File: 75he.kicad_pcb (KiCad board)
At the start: 2 copper layers, 325.3 x 138.7 mm, 395 parts, among them K1 DRV5055A3xDBZxQ1, K10 DRV5055A3xDBZxQ1, K11 DRV5055A3xDBZxQ1, K12 DRV5055A3xDBZxQ1, K13 DRV5055A3xDBZxQ1, K14 DRV5055A3xDBZxQ1, K15 DRV5055A3xDBZxQ1, K16 DRV5055A3xDBZxQ1, K17 DRV5055A3xDBZxQ1, K18 DRV5055A3xDBZxQ1, K19 DRV5055A3xDBZxQ1, K2 DRV5055A3xDBZxQ1, K20 DRV5055A3xDBZxQ1, K21 DRV5055A3xDBZxQ1, K22 DRV5055A3xDBZxQ1, K23 DRV5055A3xDBZxQ1, K24 DRV5055A3xDBZxQ1, K25 DRV5055A3xDBZxQ1, K26 DRV5055A3xDBZxQ1, K27 DRV5055A3xDBZxQ1, K28 DRV5055A3xDBZxQ1, K29 DRV5055A3xDBZxQ1, K3 DRV5055A3xDBZxQ1, K30 DRV5055A3xDBZxQ1, K31 DRV5055A3xDBZxQ1, K32 DRV5055A3xDBZxQ1, K33 DRV5055A3xDBZxQ1, K34 DRV5055A3xDBZxQ1, K35 DRV5055A3xDBZxQ1, K36 DRV5055A3xDBZxQ1, K37 DRV5055A3xDBZxQ1, K38 DRV5055A3xDBZxQ1, K39 DRV5055A3xDBZxQ1, K4 DRV5055A3xDBZxQ1, K40 DRV5055A3xDBZxQ1, K41 DRV5055A3xDBZxQ1, K42 DRV5055A3xDBZxQ1, K43 DRV5055A3xDBZxQ1, K44 DRV5055A3xDBZxQ1, K45 DRV5055A3xDBZxQ1, K46 DRV5055A3xDBZxQ1, K47 DRV5055A3xDBZxQ1, K48 DRV5055A3xDBZxQ1, K49 DRV5055A3xDBZxQ1, K5 DRV5055A3xDBZxQ1, K50 DRV5055A3xDBZxQ1, K51 DRV5055A3xDBZxQ1, K52 DRV5055A3xDBZxQ1, K53 DRV5055A3xDBZxQ1, K54 DRV5055A3xDBZxQ1, K55 DRV5055A3xDBZxQ1, K56 DRV5055A3xDBZxQ1, K57 DRV5055A3xDBZxQ1, K58 DRV5055A3xDBZxQ1, K59 DRV5055A3xDBZxQ1, K6 DRV5055A3xDBZxQ1, K60 DRV5055A3xDBZxQ1, K61 DRV5055A3xDBZxQ1, K62 DRV5055A3xDBZxQ1, K63 DRV5055A3xDBZxQ1, K64 DRV5055A3xDBZxQ1, K65 DRV5055A3xDBZxQ1, K66 DRV5055A3xDBZxQ1, K67 DRV5055A3xDBZxQ1, K68 DRV5055A3xDBZxQ1, K69 DRV5055A3xDBZxQ1, K7 DRV5055A3xDBZxQ1, K70 DRV5055A3xDBZxQ1, K71 DRV5055A3xDBZxQ1, K72 DRV5055A3xDBZxQ1, K73 DRV5055A3xDBZxQ1, K74 DRV5055A3xDBZxQ1, K75 DRV5055A3xDBZxQ1, K76 DRV5055A3xDBZxQ1, K77 DRV5055A3xDBZxQ1, K78 DRV5055A3xDBZxQ1, K79 DRV5055A3xDBZxQ1, K8 DRV5055A3xDBZxQ1, K80 DRV5055A3xDBZxQ1, K81 DRV5055A3xDBZxQ1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

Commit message: start usb
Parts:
- C172, SW_RST1: moved to B.Cu
- moved C172 115.0 mm to (147.6, 44.0)
- moved SW_RST1 86.5 mm to (147.6, 40.3), turned to -90 degrees
- moved C169 0.11 mm to (141.1, 41.4)
- moved C170 0.10 mm to (141.6, 39.9)
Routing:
- net /MCU/OSC_OUT: track 0.00 -> 6.83 mm
- net +3.3V: track 0.00 -> 5.15 mm
- net /MCU/OSC_IN: track 0.00 -> 4.32 mm
- net M6_OUT: track 216.6 -> 215.1 mm
- net M4_OUT: track 184.6 -> 185.8 mm
- net M3_OUT: track 158.8 -> 159.9 mm
- net M5_OUT: track 125.1 -> 126.2 mm

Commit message: start usb
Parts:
- added C214: 100nF, PCM_JLCPCB:C_0402, F.Cu at (72.3, -22.1)
- added J201: Connector, USB-TYPE-C-16P, Connector_USB:USB_C_Receptacle_XKB_U262-16XN-4BVC11, B.Cu at (90.4, 26.7)
- added R201: 5.1kΩ, PCM_JLCPCB:R_0402, F.Cu at (72.3, -20.2)
- added R202: 5.1kΩ, PCM_JLCPCB:R_0402, F.Cu at (72.3, -18.4)
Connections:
- U2 pad 1: unconnected-(U2-I/O1-Pad1) -> /MCU/USB_PLUG_D-
- U2 pad 2: unconnected-(U2-GND-Pad2) -> GND
- U2 pad 3: unconnected-(U2-I/O2-Pad3) -> /MCU/USB_PLUG_D+
- U2 pad 4: unconnected-(U2-I/O2-Pad4) -> /MCU/USB_D+
- U2 pad 5: unconnected-(U2-VBUS-Pad5) -> VBUS
- U2 pad 6: unconnected-(U2-I/O1-Pad6) -> /MCU/USB_D-

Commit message: start analog ldo layout
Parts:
- removed C185: 470nF, PCM_JLCPCB:C_0603
- removed C191, C192: 10uF, PCM_JLCPCB:C_0805
- removed C193: 2.2nF, PCM_JLCPCB:C_0402
- removed C194, C195, C196, C197, C198: 22uF, PCM_JLCPCB:C_0805
- removed FB1: 8.5Ω@100MHz, PCM_JLCPCB:FB_0603
- removed L1: 2.2uH, Inductor_SMD:L_1210_3225Metric
- removed R2: 19.6kΩ, Resistor_SMD:R_0402_1005Metric
- removed R3: 4.87kΩ, PCM_JLCPCB:R_0603
- removed U3: TPS62913, Package_DFN_QFN:Texas_RPU0010A_VQFN-HR-10_2x2mm_P0.5mm
- moved U4 58.7 mm to (12.4, -21.1)
- moved C182 57.9 mm to (16.6, -21.8)
- moved C184 56.9 mm to (12.1, -25.4)
- moved C183 56.2 mm to (16.1, -24.5), turned to 90 degrees
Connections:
- C183 pad 1: +4V -> VBUS
- C186 pad 1: +4V -> VBUS
- U1 pad 85: unconnected-(U1-PD4-Pad85) -> M_SEL_0
- U1 pad 86: unconnected-(U1-PD5-Pad86) -> M_SEL_1
- U1 pad 87: unconnected-(U1-PD6-Pad87) -> M_SEL_2
- U4 pad 13: +4V -> VBUS
- U4 pad 15: +4V -> VBUS
- U4 pad 16: +4V -> VBUS
- U5 pad 3: +4V -> VBUS
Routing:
- net M1_OUT: track 17.4 -> 18.3 mm
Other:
- board size 325.3 x 138.7 mm -> 317.6 x 131.8 mm

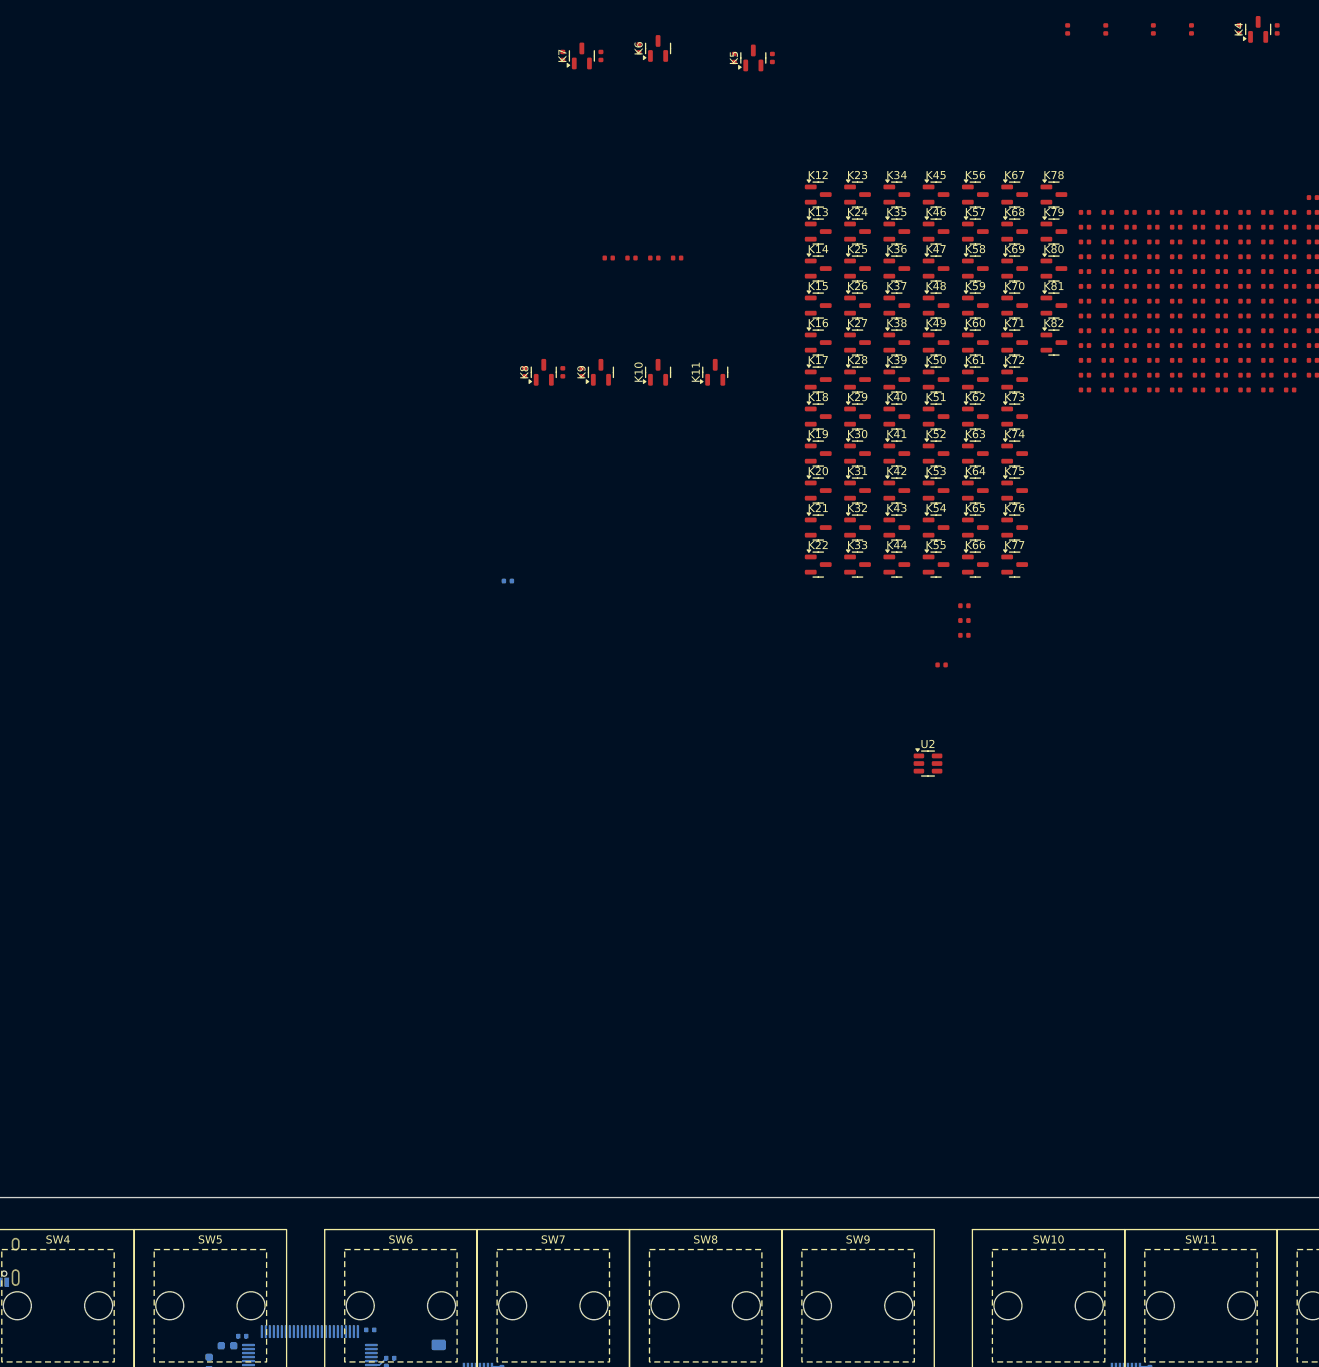
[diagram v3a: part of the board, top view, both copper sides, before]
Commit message: start placing sensors
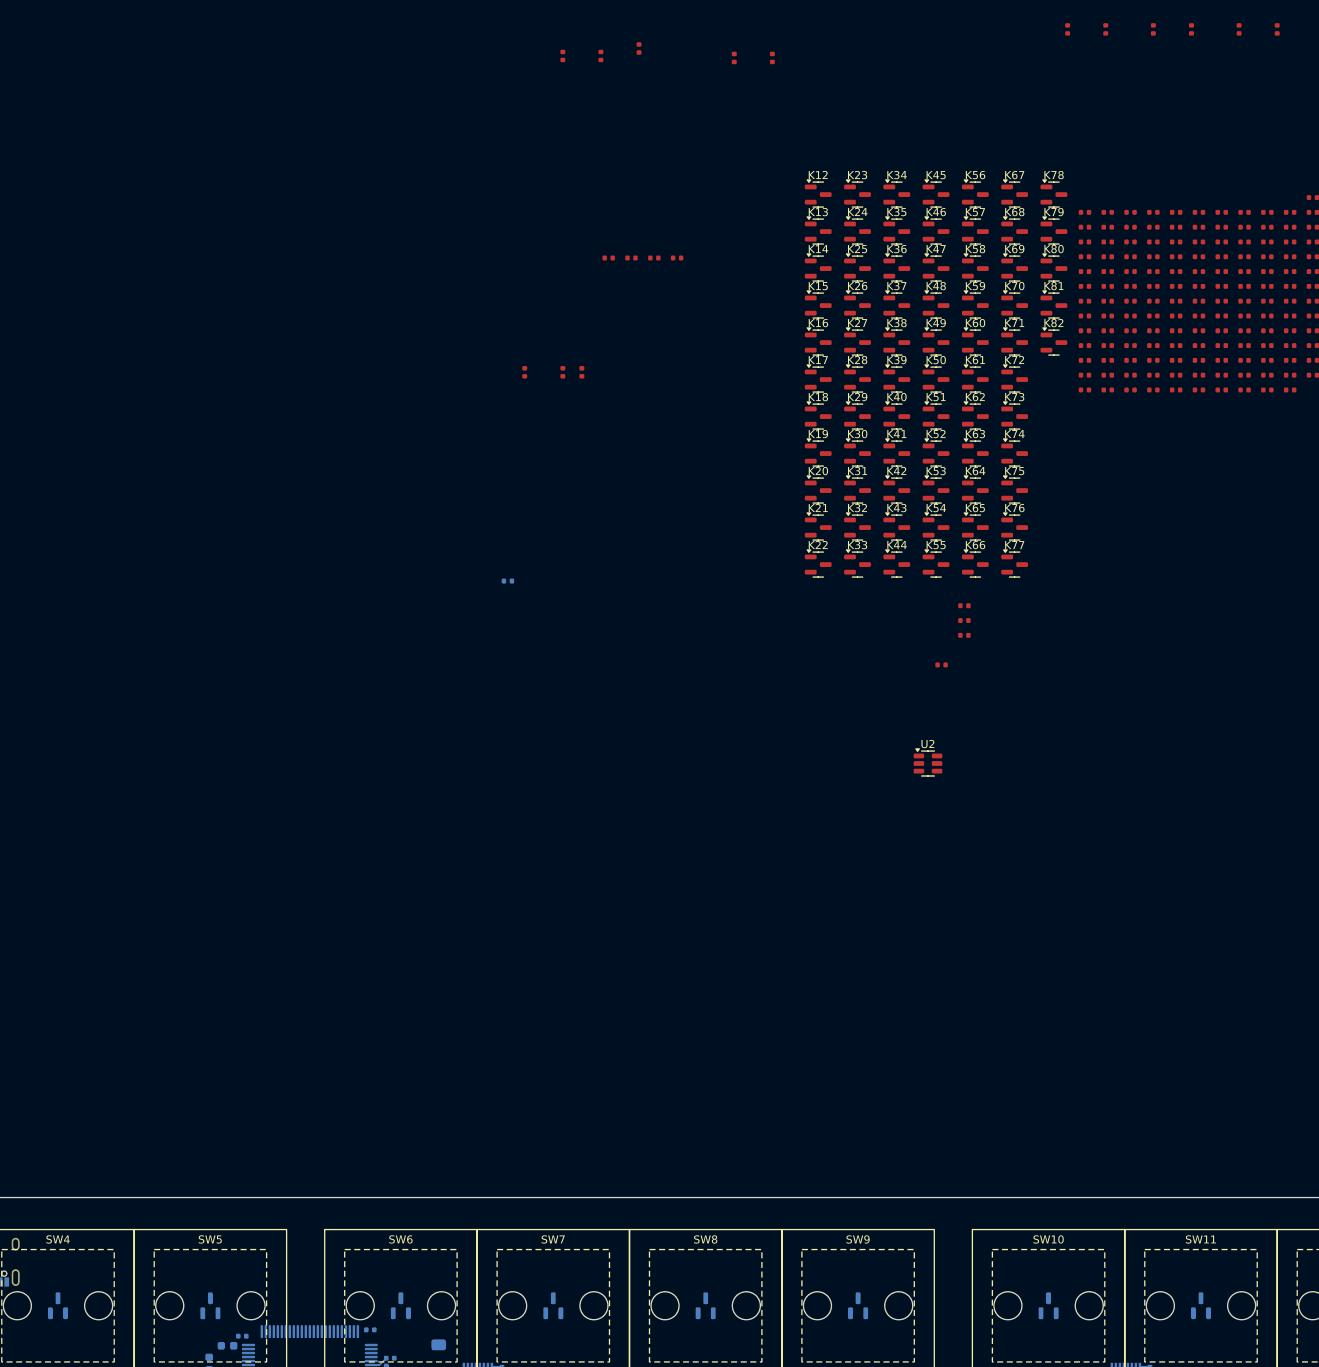
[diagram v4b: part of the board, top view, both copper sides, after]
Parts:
- K10, K11, K4, K5, K6, K7, K8, K9: moved to B.Cu
- moved K4 219.0 mm to (100.0, 33.3)
- moved K5 170.1 mm to (119.1, 33.3)
- moved K6 160.4 mm to (142.9, 33.3)
- moved K7 156.3 mm to (161.9, 33.3)
- moved K11 131.5 mm to (242.9, 33.3)
- moved K10 126.5 mm to (223.8, 33.3)
- moved K9 121.0 mm to (200.0, 33.3)
- moved K8 118.4 mm to (181.0, 33.3)

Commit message: start placing sensors
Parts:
- K12, K13, K14, K15, K16, K17, K18, K19, K20, K21, K22: moved to B.Cu
- moved K21 243.1 mm to (-11.0, 65.1), turned to 180 degrees
- moved K22 243.1 mm to (-11.0, 69.8), turned to 180 degrees
- moved K15 216.3 mm to (38.1, 57.1), turned to 90 degrees
- moved K16 199.5 mm to (57.1, 57.1), turned to 90 degrees
- moved K17 183.3 mm to (76.2, 57.1), turned to 90 degrees
- moved K14 169.9 mm to (304.8, 33.3), turned to 90 degrees
- moved K18 167.8 mm to (95.2, 57.1), turned to 90 degrees
- moved K13 159.4 mm to (281.0, 33.3), turned to 90 degrees
- moved K12 154.2 mm to (261.9, 33.3), turned to 90 degrees
- moved K19 153.3 mm to (114.3, 57.1), turned to 90 degrees
- moved K20 140.0 mm to (133.3, 57.1), turned to 90 degrees
